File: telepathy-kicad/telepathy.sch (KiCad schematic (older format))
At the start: 53 parts, among them P1 CONN_01X02, P2 CONN_01X04, P3 CONN_01X04, P4 CONN_01X05, P5 CONN_01X01, U1 LM7805, U2 ad8630, U3 DIL18, U4 ADG409, U5 DIL8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

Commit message: updated board for cnc mill, added millproject file for pcb2gcode
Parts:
- removed C1, C2, C3, C6: C, symbol C
- added C1, C2, C3, C6: CP, symbol CP
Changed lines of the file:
@@
-EESchema Schematic File Version 2  date Sun 22 Mar 2015 11:40:35 AM CDT
+EESchema Schematic File Version 2  date Mon 23 Mar 2015 10:40:53 AM CDT
 LIBS:MODULE34
 LIBS:DIL28
@@
 Sheet 1 1
 Title ""
-Date "22 mar 2015"
+Date "23 mar 2015"
 Rev ""
 Comp ""
@@
 Comment4 ""
 $EndDescr
+$Comp
+L CP C6
+U 1 1 55103357
+P 8750 7100
+F 0 "C6" H 8800 7200 50  0000 L CNN
+F 1 "CP" H 8800 7000 50  0000 L CNN
+	1    8750 7100
+	0    -1   -1   0
+$EndComp
+$Comp
+L CP C3
+U 1 1 551032A5
+P 3900 9700
+F 0 "C3" H 3950 9800 50  0000 L CNN
+F 1 "CP" H 3950 9600 50  0000 L CNN
+	1    3900 9700
+	1    0    0    -1
+$EndComp
+$Comp
+L CP C1
+U 1 1 5510329C
+P 2550 7250
+F 0 "C1" H 2600 7350 50  0000 L CNN
+F 1 "CP" H 2600 7150 50  0000 L CNN
+	1    2550 7250
+	1    0    0    -1
+$EndComp
+$Comp
+L CP C2
+U 1 1 55103297
+P 3550 7250
+F 0 "C2" H 3600 7350 50  0000 L CNN
+F 1 "CP" H 3600 7150 50  0000 L CNN
+	1    3550 7250
+	1    0    0    -1
+$EndComp
 Wire Wire Line
 	3550 8650 2400 8650
@@
 $EndComp
 $Comp
-L C C6
-U 1 1 550BF8D5
-P 8750 7100
-F 0 "C6" H 8800 7200 50  0000 L CNN
-F 1 "C" H 8800 7000 50  0000 L CNN
-	1    8750 7100
-	0    -1   -1   0
-$EndComp
-$Comp
 L R R10
 U 1 1 550BF8EE
@@
 F 1 "R" V 2407 9751 50  0000 C CNN
 	1    2400 9750
-	1    0    0    -1
-$EndComp
-$Comp
-L C C3
-U 1 1 550BFAF6
-P 3900 9700
-F 0 "C3" H 3950 9800 50  0000 L CNN
-F 1 "C" H 3950 9600 50  0000 L CNN
-	1    3900 9700
 	1    0    0    -1
 $EndComp
@@
 $EndComp
 $Comp
-L C C1
-U 1 1 550BFC8D
-P 2550 7250
-F 0 "C1" H 2600 7350 50  0000 L CNN
-F 1 "C" H 2600 7150 50  0000 L CNN
-	1    2550 7250
-	1    0    0    -1
-$EndComp
-$Comp
-L C C2
-U 1 1 550BFCA1
-P 3550 7250
-F 0 "C2" H 3600 7350 50  0000 L CNN
-F 1 "C" H 3600 7150 50  0000 L CNN
-	1    3550 7250
-	1    0    0    -1
-$EndComp
-$Comp
 L GND #PWR09
 U 1 1 550BFCB5
@@
 $EndComp
 $Comp
-L GNDA #PWR015
+L GNDA #PWR013
 U 1 1 550BFEF0
 P 9000 6350
-F 0 "#PWR015" H 9000 6100 60  0001 C CNN
+F 0 "#PWR013" H 9000 6100 60  0001 C CNN
 F 1 "GNDA" H 9000 6200 60  0000 C CNN
 	1    9000 6350
@@
 $EndComp
 $Comp
-L GND #PWR016
+L GND #PWR014
 U 1 1 550BFF04
 P 8450 6400
-F 0 "#PWR016" H 8450 6150 60  0001 C CNN
+F 0 "#PWR014" H 8450 6150 60  0001 C CNN
 F 1 "GND" H 8450 6250 60  0000 C CNN
 	1    8450 6400
@@
 $EndComp
 $Comp
-L +5V #PWR017
+L +5V #PWR015
 U 1 1 550BFF18
 P 8450 5200
-F 0 "#PWR017" H 8450 5050 60  0001 C CNN
+F 0 "#PWR015" H 8450 5050 60  0001 C CNN
 F 1 "+5V" H 8450 5340 60  0000 C CNN
 	1    8450 5200
@@
 $EndComp
 $Comp
-L +5V #PWR018
+L +5V #PWR016
 U 1 1 550BFF2C
 P 6000 4500
-F 0 "#PWR018" H 6000 4350 60  0001 C CNN
+F 0 "#PWR016" H 6000 4350 60  0001 C CNN
 F 1 "+5V" H 6000 4640 60  0000 C CNN
 	1    6000 4500
@@
 $EndComp
 $Comp
-L GND #PWR019
+L GND #PWR017
 U 1 1 550BFF40
 P 3450 4800
-F 0 "#PWR019" H 3450 4550 60  0001 C CNN
+F 0 "#PWR017" H 3450 4550 60  0001 C CNN
 F 1 "GND" H 3450 4650 60  0000 C CNN
 	1    3450 4800
@@
 $EndComp
 $Comp
-L +5V #PWR020
+L +5V #PWR018
 U 1 1 550BFF54
 P 3450 4500
-F 0 "#PWR020" H 3450 4350 60  0001 C CNN
+F 0 "#PWR018" H 3450 4350 60  0001 C CNN
 F 1 "+5V" H 3450 4640 60  0000 C CNN
 	1    3450 4500
@@
 $EndComp
 $Comp
-L GND #PWR021
+L GND #PWR019
 U 1 1 550BFF68
 P 5850 4550
-F 0 "#PWR021" H 5850 4300 60  0001 C CNN
+F 0 "#PWR019" H 5850 4300 60  0001 C CNN
 F 1 "GND" H 5850 4400 60  0000 C CNN
 	1    5850 4550
@@
 $EndComp
 $Comp
-L +5V #PWR022
+L +5V #PWR020
 U 1 1 550BFF86
 P 9950 1450
-F 0 "#PWR022" H 9950 1300 60  0001 C CNN
+F 0 "#PWR020" H 9950 1300 60  0001 C CNN
 F 1 "+5V" H 9950 1590 60  0000 C CNN
 	1    9950 1450
@@
 $EndComp
 $Comp
-L GND #PWR023
+L GND #PWR021
 U 1 1 550BFF9A
 P 10050 1000
-F 0 "#PWR023" H 10050 750 60  0001 C CNN
+F 0 "#PWR021" H 10050 750 60  0001 C CNN
 F 1 "GND" H 10050 850 60  0000 C CNN
 	1    10050 1000
@@
 $EndComp
 $Comp
-L +5V #PWR024
+L +5V #PWR022
 U 1 1 550C0061
 P 13150 4450
-F 0 "#PWR024" H 13150 4300 60  0001 C CNN
+F 0 "#PWR022" H 13150 4300 60  0001 C CNN
 F 1 "+5V" H 13150 4590 60  0000 C CNN
 	1    13150 4450
@@
 $EndComp
 $Comp
-L GND #PWR025
+L GND #PWR023
 U 1 1 550C0089
 P 13150 5300
-F 0 "#PWR025" H 13150 5050 60  0001 C CNN
+F 0 "#PWR023" H 13150 5050 60  0001 C CNN
 F 1 "GND" H 13150 5150 60  0000 C CNN
 	1    13150 5300
@@
 $EndComp
 $Comp
-L +5V #PWR026
+L +5V #PWR024
 U 1 1 550C028A
 P 8300 6800
-F 0 "#PWR026" H 8300 6650 60  0001 C CNN
+F 0 "#PWR024" H 8300 6650 60  0001 C CNN
 F 1 "+5V" H 8300 6940 60  0000 C CNN
 	1    8300 6800
@@
 $EndComp
 $Comp
-L GND #PWR027
+L GND #PWR025
 U 1 1 550C029E
 P 8300 7700
-F 0 "#PWR027" H 8300 7450 60  0001 C CNN
+F 0 "#PWR025" H 8300 7450 60  0001 C CNN
 F 1 "GND" H 8300 7550 60  0000 C CNN
 	1    8300 7700
@@
 $EndComp
 $Comp
-L GND #PWR028
+L GND #PWR026
 U 1 1 550C065C
 P 2400 10150
-F 0 "#PWR028" H 2400 9900 60  0001 C CNN
+F 0 "#PWR026" H 2400 9900 60  0001 C CNN
 F 1 "GND" H 2400 10000 60  0000 C CNN
 	1    2400 10150
@@
 $EndComp
 $Comp
-L GNDA #PWR029
+L GNDA #PWR027
 U 1 1 550C0AE6
 P 9200 8200
-F 0 "#PWR029" H 9200 7950 60  0001 C CNN
+F 0 "#PWR027" H 9200 7950 60  0001 C CNN
 F 1 "GNDA" H 9200 8050 60  0000 C CNN
 	1    9200 8200
@@
 $EndComp
 $Comp
-L GNDA #PWR030
+L GNDA #PWR028
 U 1 1 550C0FFD
 P 6150 6400
-F 0 "#PWR030" H 6150 6150 60  0001 C CNN
+F 0 "#PWR028" H 6150 6150 60  0001 C CNN
 F 1 "GNDA" H 6150 6250 60  0000 C CNN
 	1    6150 6400
@@
 $EndComp
 $Comp
-L GNDA #PWR031
+L GNDA #PWR029
 U 1 1 550C1011
 P 6150 7950
-F 0 "#PWR031" H 6150 7700 60  0001 C CNN
+F 0 "#PWR029" H 6150 7700 60  0001 C CNN
 F 1 "GNDA" H 6150 7800 60  0000 C CNN
 	1    6150 7950
@@
 $EndComp
 $Comp
-L GND #PWR032
+L GND #PWR030
 U 1 1 550C3062
 P 10800 7450
-F 0 "#PWR032" H 10800 7200 60  0001 C CNN
+F 0 "#PWR030" H 10800 7200 60  0001 C CNN
 F 1 "GND" H 10800 7300 60  0000 C CNN
 	1    10800 7450
@@
 $EndComp
 $Comp
-L GND #PWR033
+L GND #PWR031
 U 1 1 550C3A5A
 P 10050 4500
-F 0 "#PWR033" H 10050 4250 60  0001 C CNN
+F 0 "#PWR031" H 10050 4250 60  0001 C CNN
 F 1 "GND" H 10050 4350 60  0000 C CNN
 	1    10050 4500
@@
 $EndComp
 $Comp
-L GND #PWR034
+L GND #PWR032
 U 1 1 550C3A7D
 P 15650 5600
-F 0 "#PWR034" H 15650 5350 60  0001 C CNN
+F 0 "#PWR032" H 15650 5350 60  0001 C CNN
 F 1 "GND" H 15650 5450 60  0000 C CNN
 	1    15650 5600
@@
 $EndComp
 $Comp
-L GND #PWR035
+L GND #PWR033
 U 1 1 550C6BF0
 P 9850 3850
-F 0 "#PWR035" H 9850 3600 60  0001 C CNN
+F 0 "#PWR033" H 9850 3600 60  0001 C CNN
 F 1 "GND" H 9850 3700 60  0000 C CNN
 	1    9850 3850
@@
 $EndComp
 $Comp
-L GNDA #PWR036
+L GNDA #PWR034
 U 1 1 550C6F27
 P 8450 7550
-F 0 "#PWR036" H 8450 7300 60  0001 C CNN
+F 0 "#PWR034" H 8450 7300 60  0001 C CNN
 F 1 "GNDA" H 8450 7400 60  0000 C CNN
 	1    8450 7550
@@
 $EndComp
 $Comp
-L GNDA #PWR037
+L GNDA #PWR035
 U 1 1 550C93EA
 P 6000 10300
-F 0 "#PWR037" H 6000 10050 60  0001 C CNN
+F 0 "#PWR035" H 6000 10050 60  0001 C CNN
 F 1 "GNDA" H 6000 10150 60  0000 C CNN
 	1    6000 10300
@@
 $EndComp
 $Comp
-L GNDA #PWR038
+L GNDA #PWR036
 U 1 1 550C95EA
 P 8300 10300
-F 0 "#PWR038" H 8300 10050 60  0001 C CNN
+F 0 "#PWR036" H 8300 10050 60  0001 C CNN
 F 1 "GNDA" H 8300 10150 60  0000 C CNN
 	1    8300 10300
@@
 $EndComp
 $Comp
-L GNDA #PWR039
+L GNDA #PWR037
 U 1 1 550C9D29
 P 9150 9400
-F 0 "#PWR039" H 9150 9150 60  0001 C CNN
+F 0 "#PWR037" H 9150 9150 60  0001 C CNN
 F 1 "GNDA" H 9150 9250 60  0000 C CNN
 	1    9150 9400
@@
 $EndComp
 $Comp
-L +5V #PWR040
+L +5V #PWR038
 U 1 1 550CBAD9
 P 3100 8450
-F 0 "#PWR040" H 3100 8300 60  0001 C CNN
+F 0 "#PWR038" H 3100 8300 60  0001 C CNN
 F 1 "+5V" H 3100 8590 60  0000 C CNN
 	1    3100 8450
@@
 $EndComp
 $Comp
-L GND #PWR041
+L GND #PWR039
 U 1 1 550CBAED
 P 2600 6150
-F 0 "#PWR041" H 2600 5900 60  0001 C CNN
+F 0 "#PWR039" H 2600 5900 60  0001 C CNN
 F 1 "GND" H 2600 6000 60  0000 C CNN
 	1    2600 6150
@@
 $EndComp
 $Comp
-L +BATT #PWR042
+L +BATT #PWR040
 U 1 1 550CA077
 P 2550 6600
-F 0 "#PWR042" H 2550 6450 60  0001 C CNN
+F 0 "#PWR040" H 2550 6450 60  0001 C CNN
 F 1 "+BATT" H 2550 6740 60  0000 C CNN
 	1    2550 6600
@@
 $EndComp
 $Comp
-L +BATT #PWR043
+L +BATT #PWR041
 U 1 1 550CA08B
 P 2600 5150
-F 0 "#PWR043" H 2600 5000 60  0001 C CNN
+F 0 "#PWR041" H 2600 5000 60  0001 C CNN
 F 1 "+BATT" H 2600 5290 60  0000 C CNN
 	1    2600 5150
@@
 $EndComp
 $Comp
-L +5V #PWR044
+L +5V #PWR042
 U 1 1 550CA1D7
 P 12500 6250
-F 0 "#PWR044" H 12500 6100 60  0001 C CNN
+F 0 "#PWR042" H 12500 6100 60  0001 C CNN
 F 1 "+5V" H 12500 6390 60  0000 C CNN
 	1    12500 6250

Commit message: increase pad and rack widths , added missing connection
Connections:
- wire segments 237 -> 239

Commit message: made board a little smaller
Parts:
- removed P1: CONN_01X02, symbol CONN_01X02
- removed P2, P3: CONN_01X04, symbol CONN_01X04
- removed P4: CONN_01X05, symbol CONN_01X05
- removed P5: CONN_01X01, symbol CONN_01X01
- added K1: CONN_3, symbol CONN_3
- added P1: CONN_2, symbol CONN_2
- added P2, P3, P4, P5: CONN_4, symbol CONN_4
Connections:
- wire segments 239 -> 244
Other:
- moved on the sheet: D8

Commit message: added a couple capacitors
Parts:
- added C17: C, symbol C
- added R16: R, symbol R
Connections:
- net GNDA: now also R16.2
- net at R11.1, U2.13 (-), U6.5 (PA0): now also C17.2
- net at R11.2, U2.14, U8.2 (PIN2): now also C17.1, R16.1

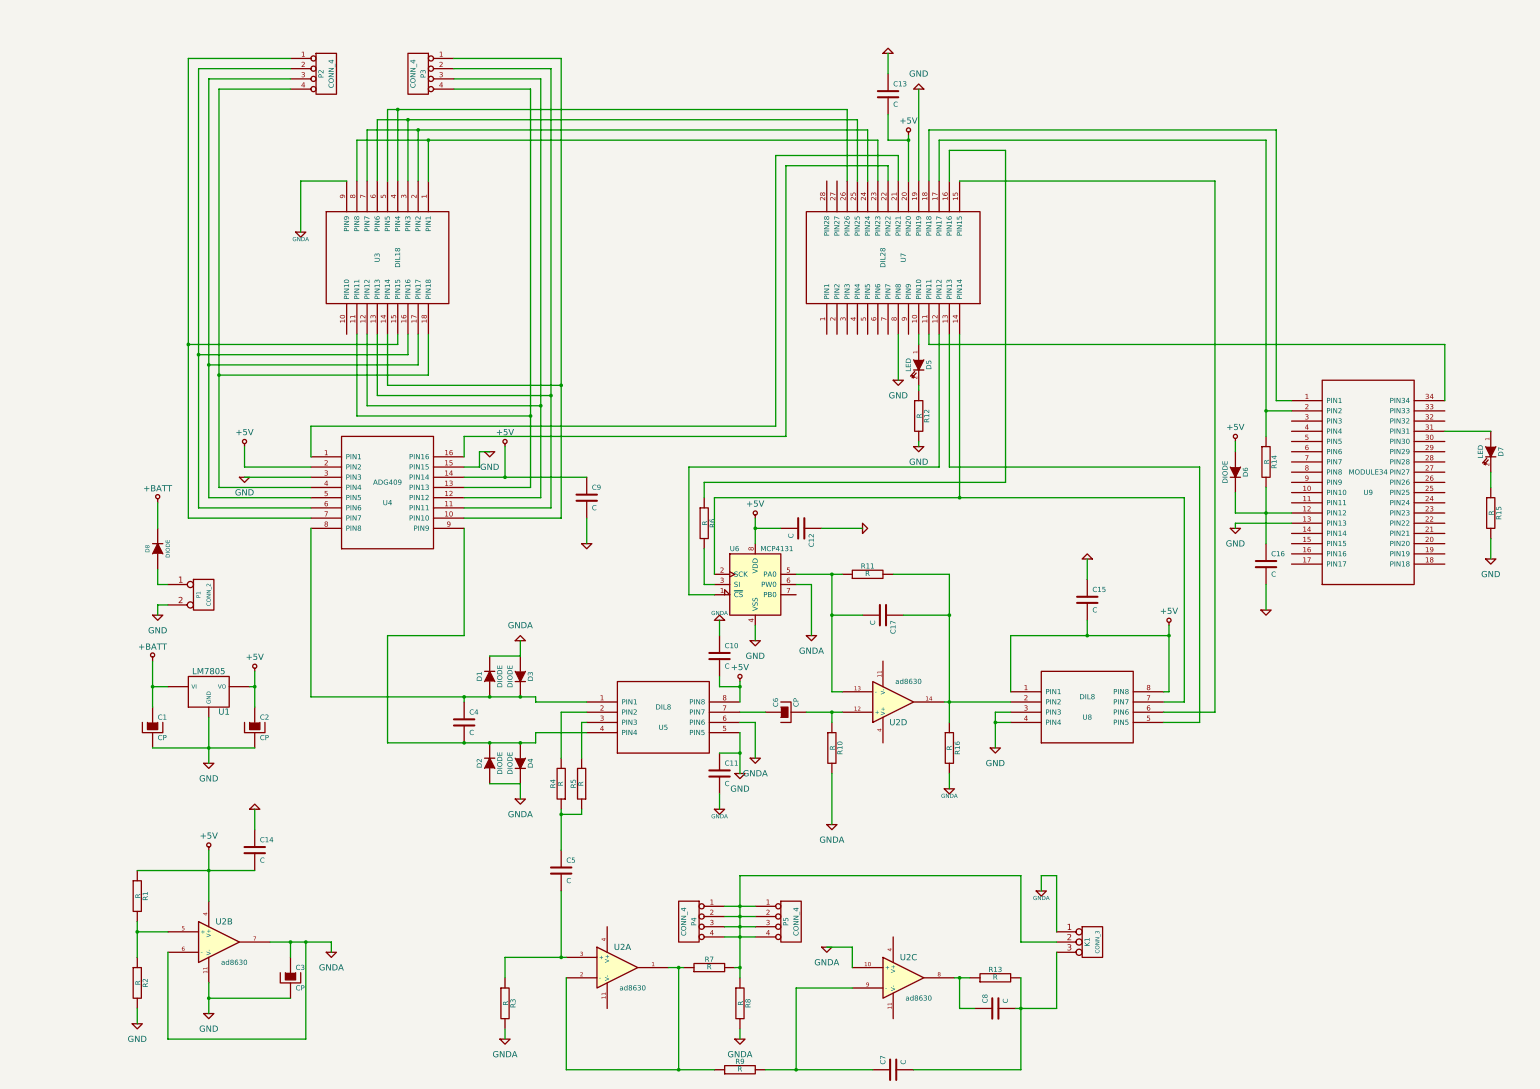
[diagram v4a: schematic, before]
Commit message: update schematic
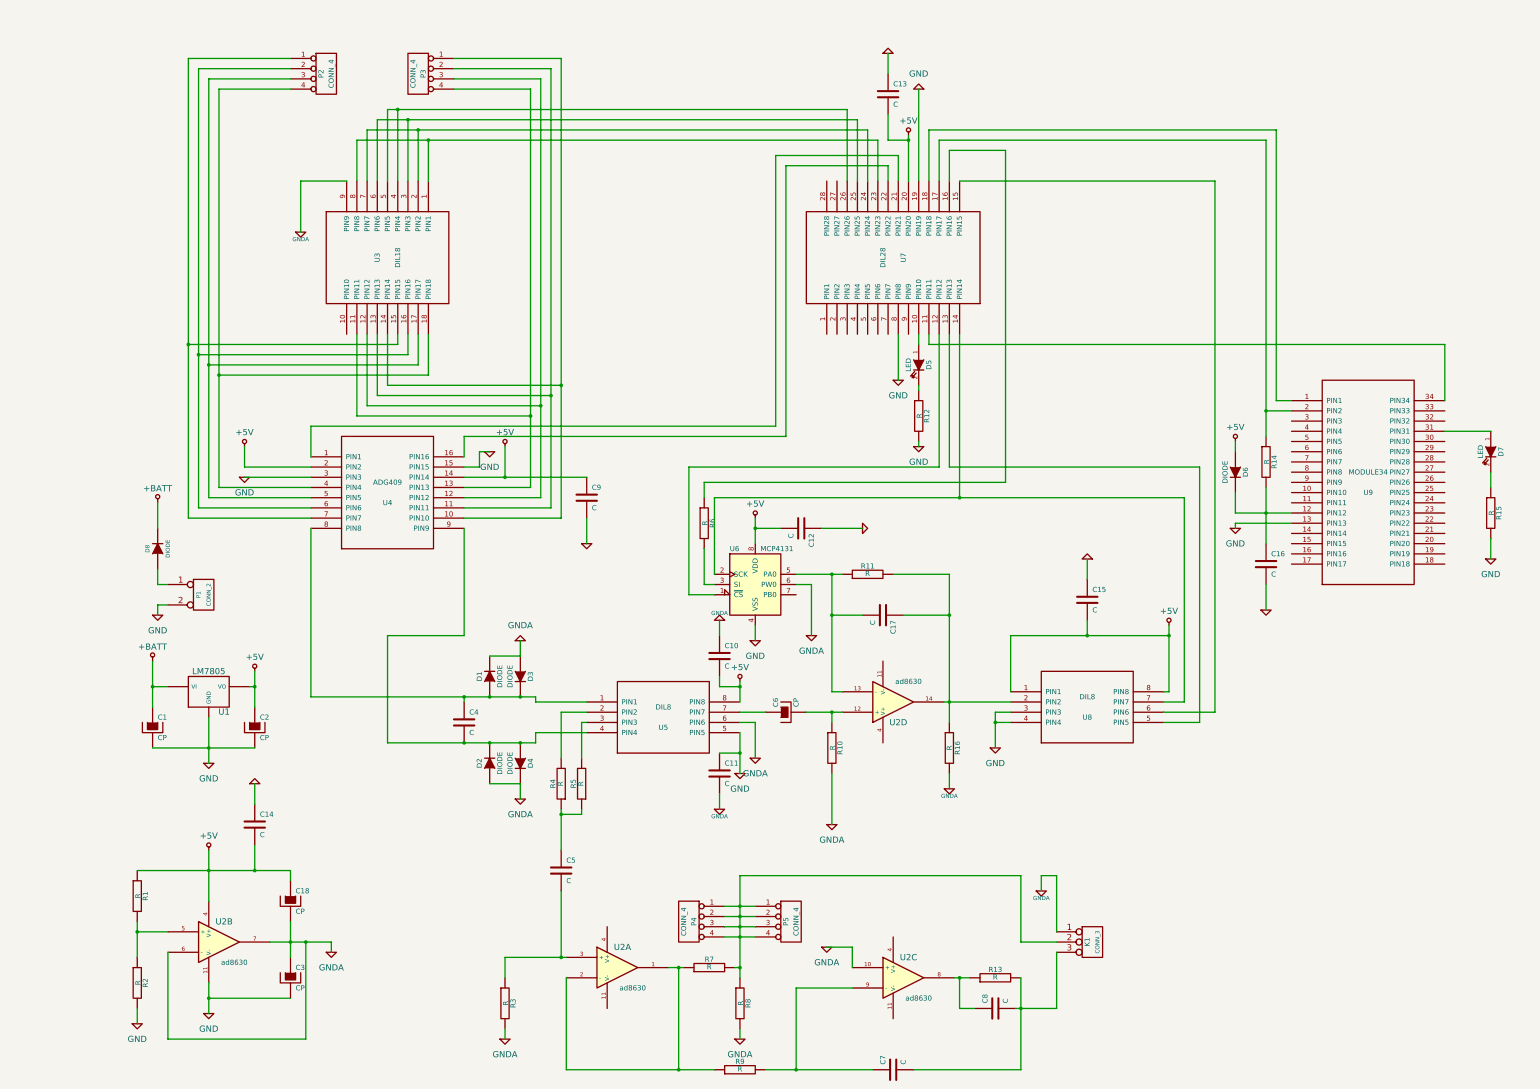
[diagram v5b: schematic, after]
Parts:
- added C18: CP, symbol CP
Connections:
- net +5V: now also C18.1
- net GNDA: now also C18.2
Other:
- moved on the sheet: C14

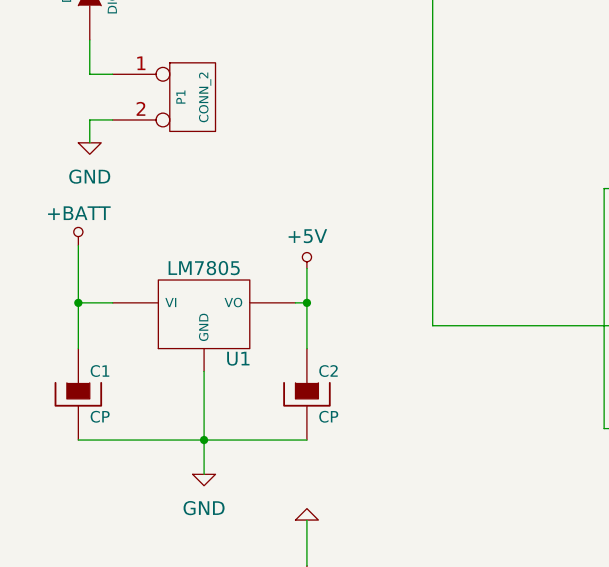
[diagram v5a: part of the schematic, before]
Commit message: changed footprints
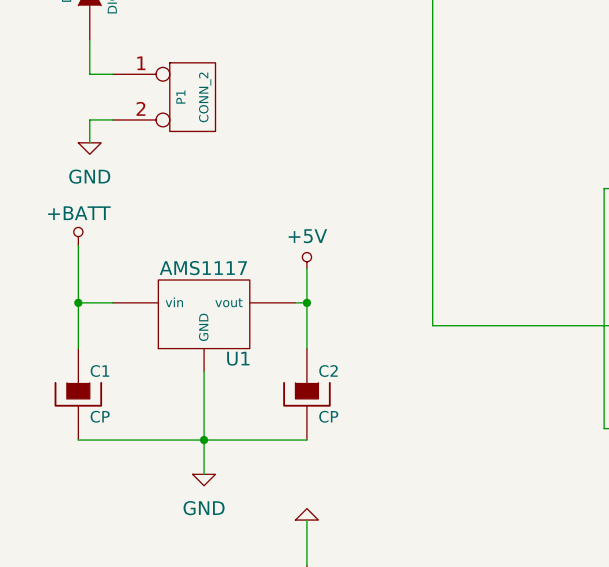
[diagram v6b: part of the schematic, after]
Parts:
- removed U1: LM7805, symbol LM7805
- added U1: AMS1117, symbol AMS1117
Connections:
- net +5V: now also U1.2 (vout)
- net +BATT: now also U1.3 (vin)
- net GND: now also U1.1 (GND)
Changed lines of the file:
@@
-EESchema Schematic File Version 2  date Sun 29 Mar 2015 12:13:41 PM CDT
+EESchema Schematic File Version 2  date Mon 30 Mar 2015 09:23:29 PM CDT
 LIBS:MODULE34
 LIBS:DIL28
@@
 LIBS:valves
 LIBS:mcp41x1
+LIBS:ams1117
 LIBS:telepathy-cache
 EELAYER 25  0
@@
 Sheet 1 1
 Title ""
-Date "29 mar 2015"
+Date "31 mar 2015"
 Rev ""
 Comp ""
@@
 Comment4 ""
 $EndDescr
+$Comp
+L AMS1117 U1
+U 1 1 5519F739
+P 3100 6900
+F 0 "U1" H 3250 6704 60  0000 C CNN
+F 1 "AMS1117" H 3100 7100 60  0000 C CNN
+	1    3100 6900
+	1    0    0    -1
+$EndComp
 Connection ~ 3550 8650
 Wire Wire Line
@@
 	1    0    0    -1
 $EndComp
-$Comp
-L LM7805 U1
-U 1 1 550BACB7
-P 3100 6900
-F 0 "U1" H 3250 6704 60  0000 C CNN
-F 1 "LM7805" H 3100 7100 60  0000 C CNN
-	1    3100 6900
-	1    0    0    -1
-$EndComp

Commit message: adjusted footprints,added filter components
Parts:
- added C19: C, symbol C
- added R17: R, symbol R
- C6: symbol CP -> C
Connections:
- net GNDA: now also C19.2
- net at R10.1, U2.12 (+): now also C19.1, R17.1; no longer C6.2
- new net: C6.2, R17.2
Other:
- moved on the sheet: C15, C16, C17, D6, D7, R10, R11, R14, R15, R16, U2D, U8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

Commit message: first version
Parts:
- removed D6: DIODE, symbol DIODE
- removed U3: DIL18, MODULE, symbol DIL18
- added Q1, Q2, Q3, Q4, Q5, Q6, Q7, Q8: NPN, symbol NPN
- added R18, R19, R20, R21, R22: R, symbol R
- added U10: 7833, symbol 7805
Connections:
- net +5V: now also U10.VI
- net GND: now also U10.GND
- net GNDA: now also Q1.2 (E), Q2.2 (E), Q3.2 (E), Q4.2 (E), Q5.2 (E), Q6.2 (E), Q7.2 (E), Q8.2 (E)
- net at U4.10 (PIN10): now also P3.4 (P4), Q8.3 (C); no longer P3.1 (P1)
- net at U4.11 (PIN11): now also P3.3 (P3), Q6.3 (C); no longer P3.2 (P2)
- net at U4.12 (PIN12): now also P3.2 (P2), Q4.3 (C); no longer P3.3 (P3)
- net at U4.13 (PIN13): now also P3.1 (P1), Q2.3 (C); no longer P3.4 (P4)
- net at U4.4 (PIN4): now also P2.1 (P1), Q1.3 (C); no longer P2.4 (P4)
- net at U4.5 (PIN5): now also P2.2 (P2), Q3.3 (C); no longer P2.3 (P3)
- net at U4.6 (PIN6): now also P2.3 (P3), Q5.3 (C); no longer P2.2 (P2)
- net at U4.7 (PIN7): now also P2.4 (P4), Q7.3 (C); no longer P2.1 (P1)
- net at U7.23 (PIN23): now also R19.1
- net at U7.24 (PIN24): now also R20.1
- net at U7.25 (PIN25): now also R21.1
- net at U7.26 (PIN26): now also R22.1
- net at U7.11 (PIN11), U9.34 (PIN34): now also R18.2
- net +3.3V: now reaches C16.1, R14.2, U9.12 (PIN12)
- net +3.3V: now also R18.1, U10.VO
- new net: Q7.1 (B), Q8.1 (B), R20.2
- new net: Q5.1 (B), Q6.1 (B), R19.2
- new net: Q1.1 (B), Q2.1 (B), R21.2
- new net: Q3.1 (B), Q4.1 (B), R22.2
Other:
- note added: "these pins are swapped because the routing was difficult \npin 23 controls channel 3\npin 24 controls channel 4\npin 25 controls channel 1\npin 26 controls channel 2"
- moved on the sheet: C1, C2, D8, P1, U1
